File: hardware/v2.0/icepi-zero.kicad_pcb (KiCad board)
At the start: 4 copper layers, 65 x 30 mm, 165 parts, among them IC1 IS42S16160J-6BLI, J1 Conn_02x20_Counter_Clockwise, J2 GPDI_C_1.3, J3 USB_C_Receptacle_USB2.0_14P, J4 USB_C_Receptacle_USB2.0_14P, J5 USB_C_Receptacle_USB2.0_14P, J6 Micro_SD_Card_Det2, SW1 SW_Push, SW2 SW_Push, U1 ECP5-CABGA256, U10 TPD2EUSB30A, U12 W25Q128JVS, U2 TLV62569DBV, U3 TLV62569DBV, U4 TLV62569DBV, U5 TPD2EUSB30A, U6 PCA9306DC1, U7 TPD2EUSB30A, U8 TPD2EUSB30A, U9 FT231XQ, Y1 SG-8018CG 50.000000MHz

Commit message: Power lines
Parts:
- added C55: 22nF, Capacitor_SMD:C_0603_1608Metric, B.Cu at (169.9, 107.4)
- moved LOGO1 8.77 mm to (176.7, 107.4)
- moved C53 8.48 mm to (168.9, 103.3), turned to 0 degrees
- moved C50 4.88 mm to (168.9, 104.8), turned to 0 degrees
- moved SW2 2.27 mm to (162.3, 106.8)
- moved TP1 1.94 mm to (173.8, 103.5)
- moved C47 1.36 mm to (162.8, 111.9)
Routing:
- net +3V3: track 89.8 -> 93.5 mm, vias 28 -> 30
- net /SW1: track 8.23 -> 10.4 mm
- net /LED4: track 27.6 -> 26.2 mm
- net /LED3: track 23.4 -> 22.3 mm
- net /LED2: track 22.6 -> 21.6 mm
- net /LED1: track 18.9 -> 18.0 mm
- net GND: track 103.4 -> 102.6 mm, vias 109 -> 108
- net /USB/USB1_PULL_D-: track 17.4 -> 18.0 mm

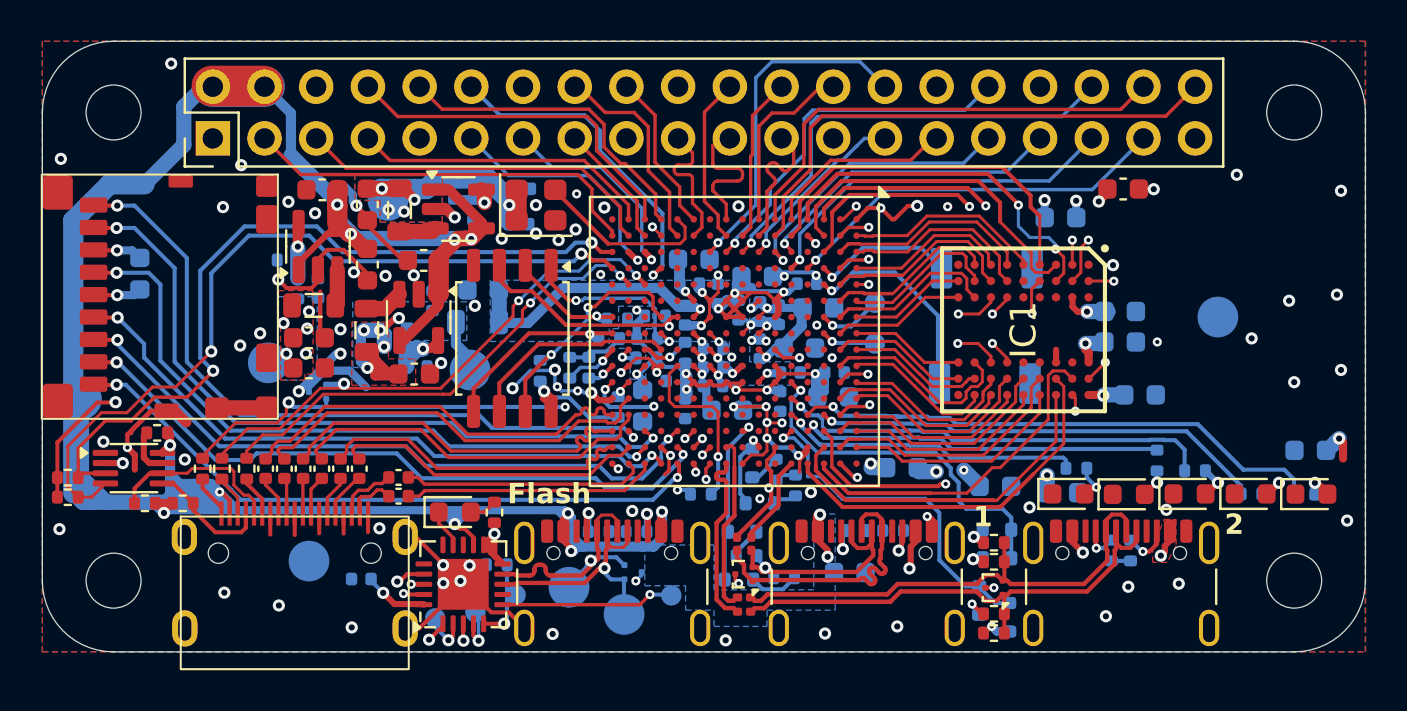
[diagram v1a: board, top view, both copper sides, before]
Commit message: Almost done power lines
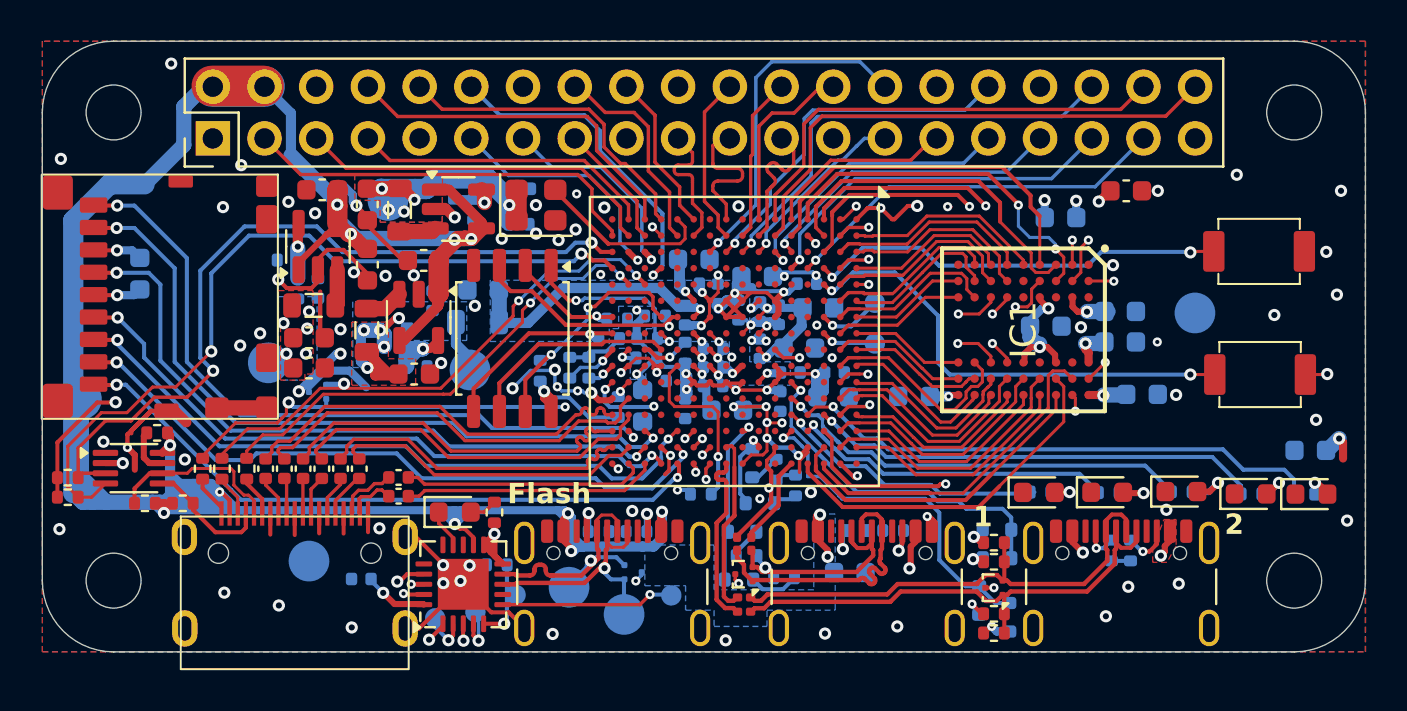
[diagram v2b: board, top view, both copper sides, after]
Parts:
- removed C55: 22nF, Capacitor_SMD:C_0603_1608Metric
- SW1, SW2: moved to F.Cu
- moved SW2 13.5 mm to (175.8, 106.4)
- moved SW1 13.4 mm to (175.8, 100.3)
- moved C49 12.3 mm to (170.0, 107.3), turned to 0 degrees
- moved LOGO1 8.93 mm to (172.1, 99.7)
- moved C48 8.22 mm to (165.3, 104.0)
- moved G*** 6.13 mm to (177.3, 106.0)
- moved C47 5.96 mm to (158.8, 107.5), turned to 180 degrees
- moved R2 2.85 mm to (168.4, 112.2), turned to 0 degrees
- moved R1 2.11 mm to (165.0, 112.2)
- moved D1 1.46 mm to (165.0, 112.2)
- moved R3 1.22 mm to (172.0, 112.1)
- moved TP1 1.14 mm to (172.6, 103.3)
- moved D2 1.06 mm to (168.3, 112.2)
- moved D3 0.41 mm to (172.0, 112.1)
- moved C46 0.17 mm to (169.2, 97.3)
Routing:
- net /SW0: track 6.75 -> 20.6 mm, vias 1 -> 2
- net /SW1: track 10.4 -> 23.3 mm, vias 1 -> 2
- net +3V3: track 93.5 -> 97.3 mm
- net /LED1: track 18.0 -> 16.0 mm
- net /LED0: track 14.8 -> 13.5 mm
- net /SDRAM/D3: track 17.4 -> 16.3 mm
- net Net-(D3-A): track 1.64 -> 2.67 mm
- net /LED2: track 21.6 -> 20.7 mm
- net /USB/USB1_PULL_D-: track 18.0 -> 17.2 mm
- net /SDRAM/D4: track 18.3 -> 17.7 mm
- net /SDRAM/D9: track 13.1 -> 12.5 mm
- net /SDRAM/D6: track 12.4 -> 13.0 mm
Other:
- board text added: "Icepi Zero v2.0"
- board text removed: "Icepi Zero v1.3"

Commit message: Power lines done
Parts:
- moved R4 0.87 mm to (174.5, 112.1)
- moved D3 0.77 mm to (171.2, 112.2)
- moved R3 0.77 mm to (171.2, 112.2)
- moved D4 0.77 mm to (174.6, 112.2)
- moved D1 0.55 mm to (164.4, 112.2)
- moved R1 0.55 mm to (164.5, 112.2)
- moved D2 0.53 mm to (167.8, 112.2)
- moved R2 0.53 mm to (167.9, 112.2)
- moved D5 0.35 mm to (178.0, 112.2)
- moved R5 0.35 mm to (177.7, 112.2)
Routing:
- net Net-(D5-A): track 0.79 -> 2.13 mm
- net /LED3: track 22.5 -> 21.3 mm
- net +3V3: track 97.3 -> 96.2 mm
- net Net-(D3-A): track 2.67 -> 1.74 mm
- net /LED4: track 26.2 -> 25.4 mm
- net /LED2: track 20.7 -> 20.0 mm
- net Net-(D2-A): track 1.13 -> 1.79 mm
- net /LED0: track 13.5 -> 12.9 mm
- net /LED1: track 16.0 -> 15.5 mm
